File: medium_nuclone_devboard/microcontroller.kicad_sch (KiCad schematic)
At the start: 1 part

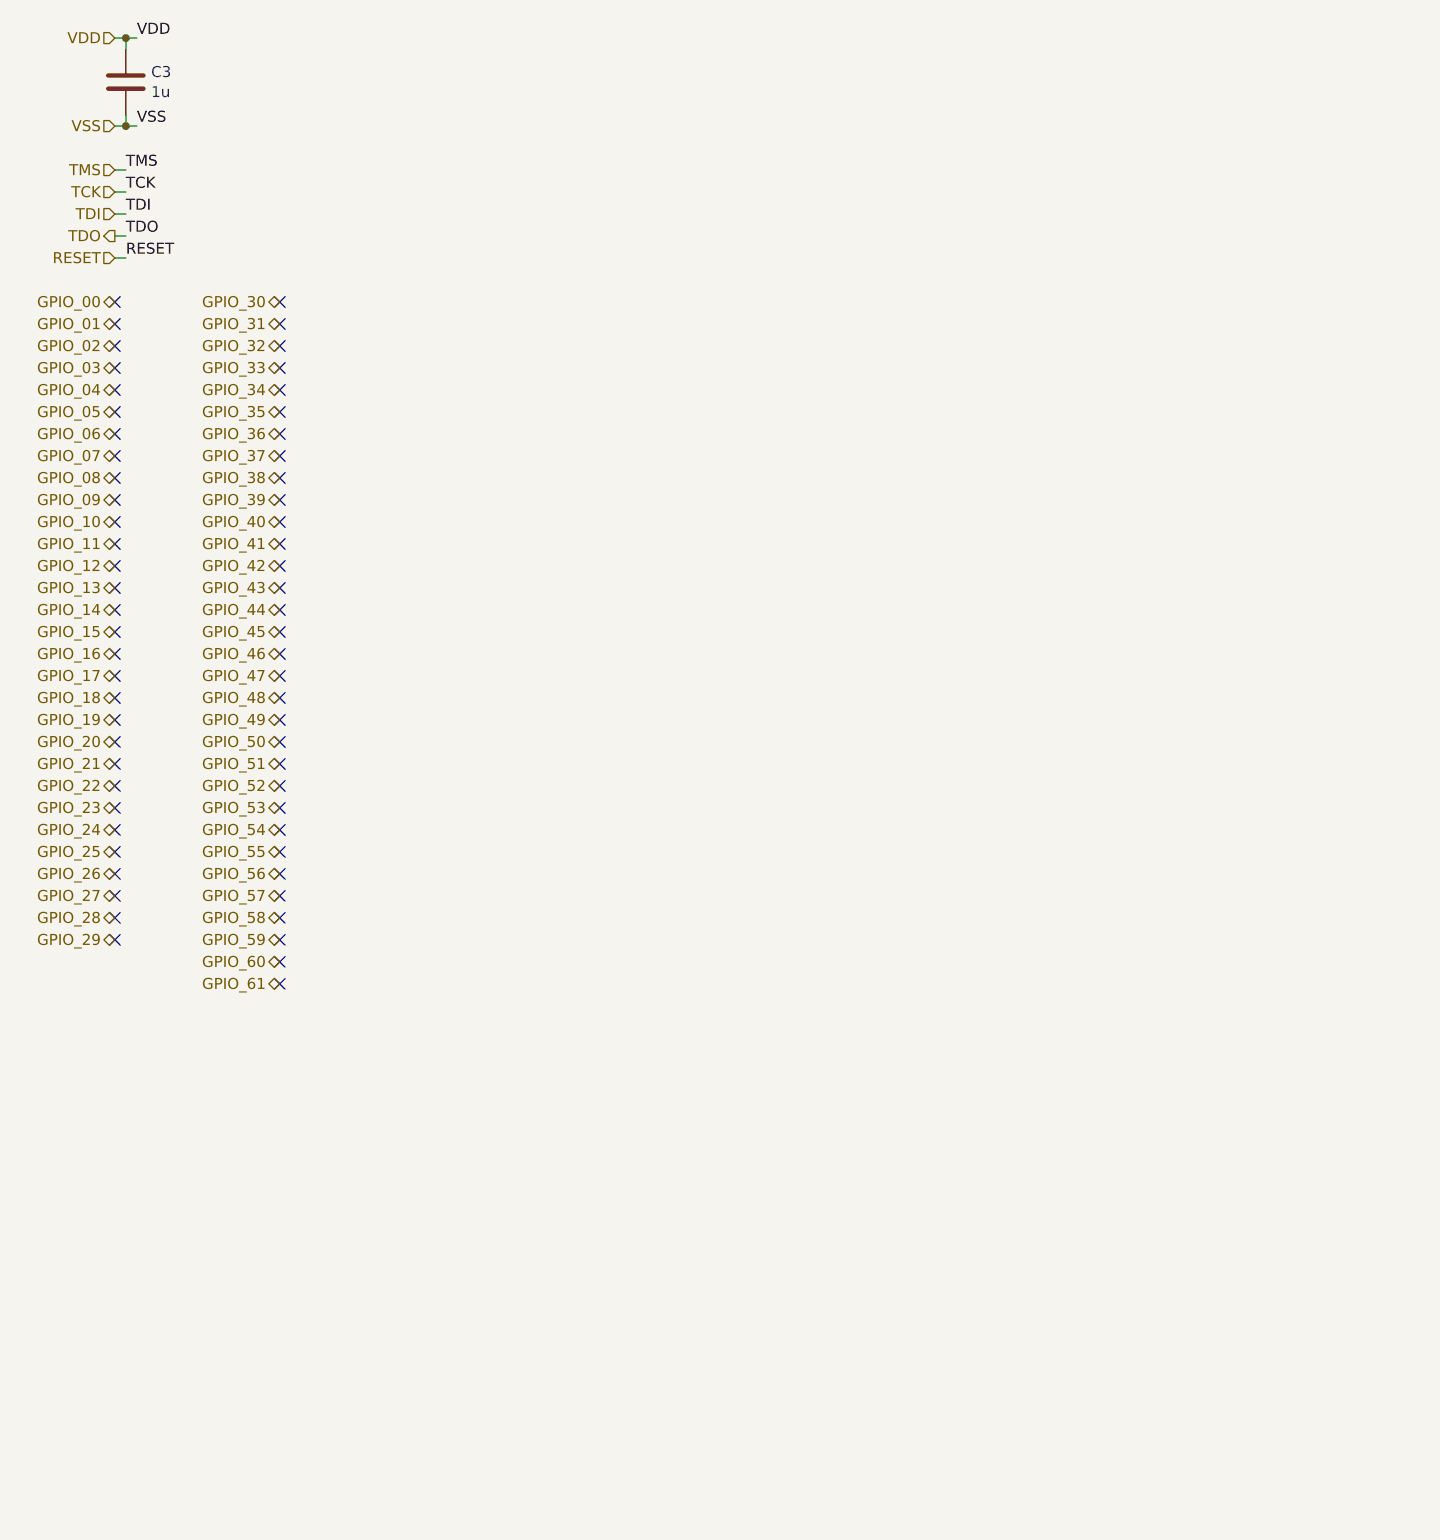
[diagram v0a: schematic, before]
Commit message: imported aisler simple design rules
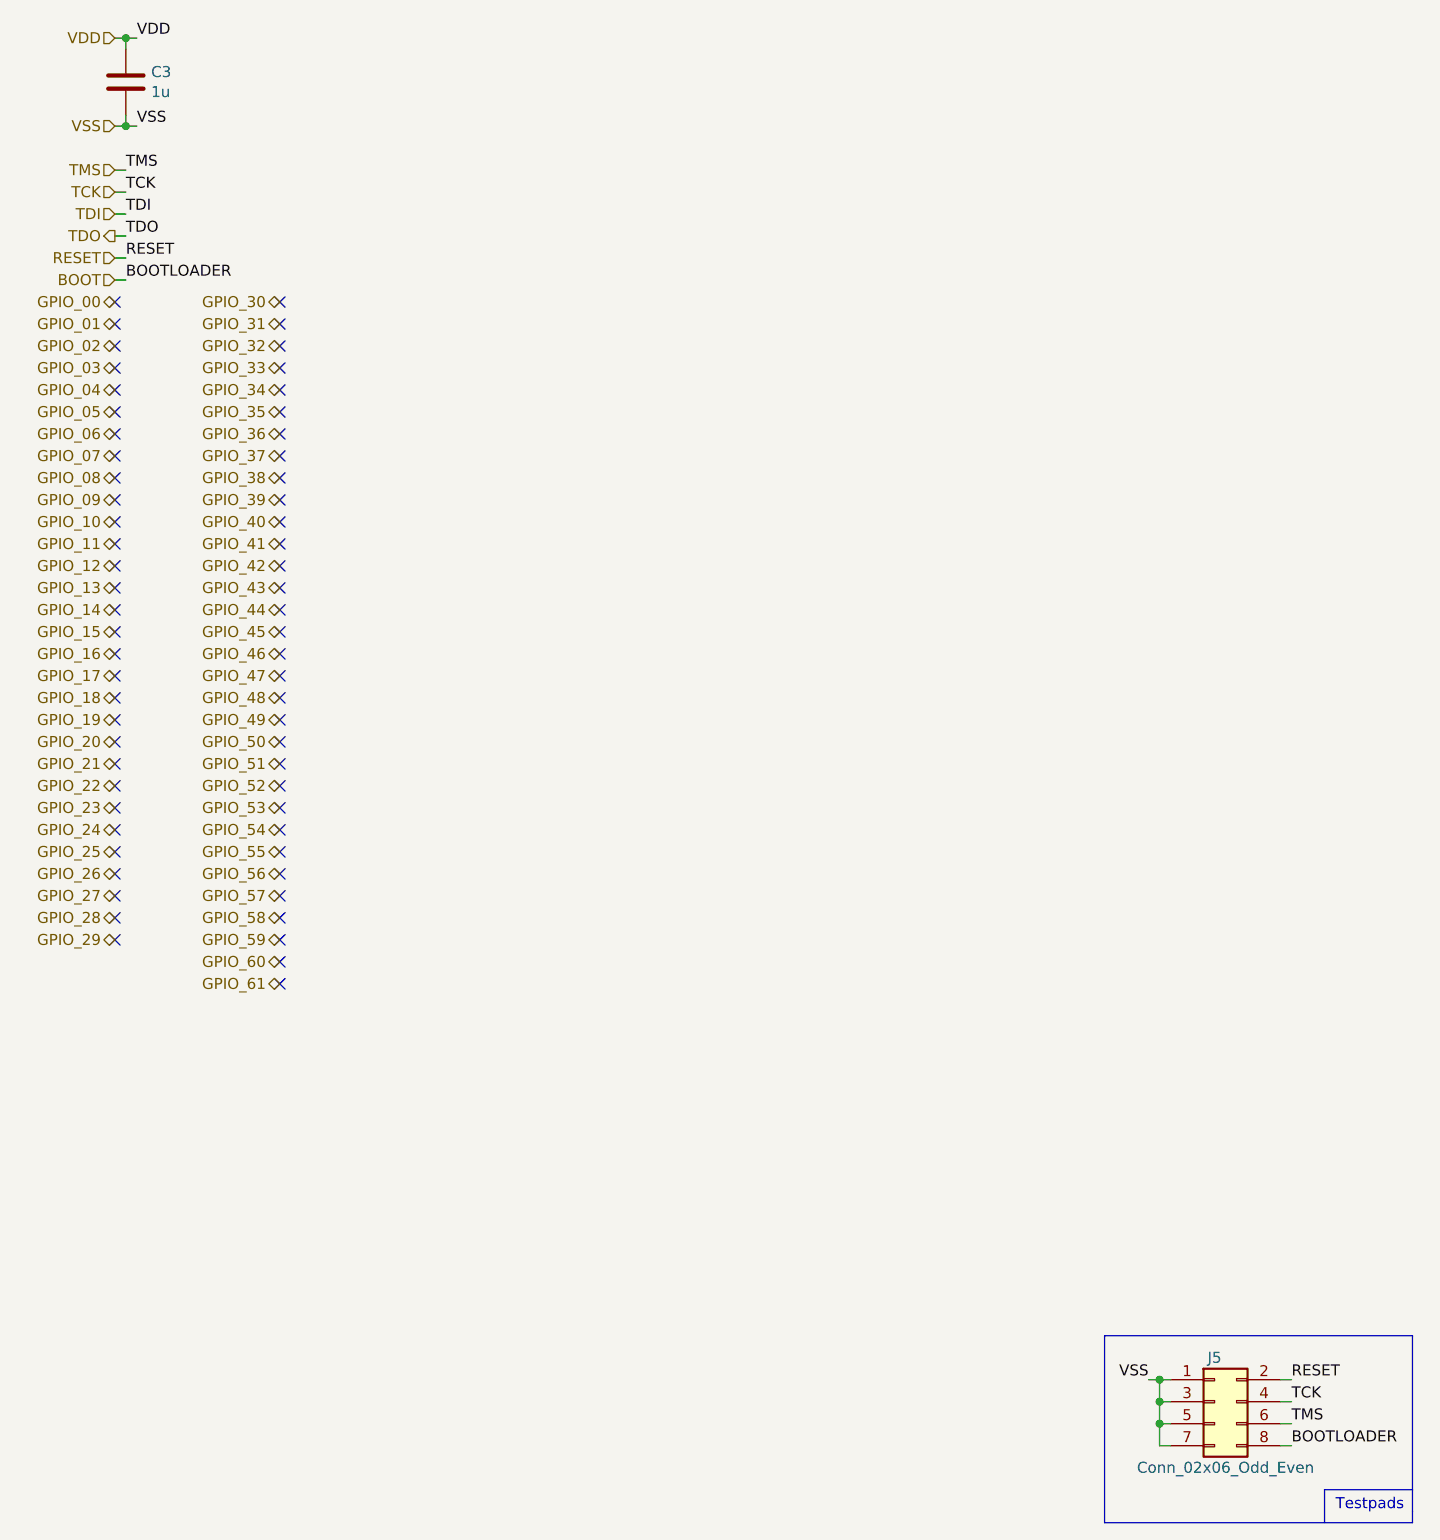
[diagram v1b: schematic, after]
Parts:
- added J5: Conn_02x06_Odd_Even, SquantorConnectors:Header-0127-2X04-H006, symbol Connector_Generic:Conn_02x04_Odd_Even
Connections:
- net RESET: now also J5.2 (Pin_2)
- net TCK: now also J5.4 (Pin_4)
- net TMS: now also J5.6 (Pin_6)
- net VSS: now also J5.1 (Pin_1), J5.3 (Pin_3), J5.5 (Pin_5), J5.7 (Pin_7)
- new net BOOT: J5.8 (Pin_8)
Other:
- note added: "Testpads"
